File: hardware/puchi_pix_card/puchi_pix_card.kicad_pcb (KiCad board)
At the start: 4 copper layers, 54 x 54 mm, 367 parts, among them J1 USB_C_Receptacle_USB2.0_16P, J2 Conn_01x04, J3 Conn_01x10, J4 Conn_01x10, Q101 AO3401A, Q102 AO3401A, Q103 AO3401A, Q104 AO3401A, Q105 AO3401A, Q106 AO3401A, Q107 AO3401A, Q108 AO3401A, Q109 AO3401A, Q110 AO3401A, Q111 AO3401A, Q112 AO3401A, Q113 AO3401A, Q114 AO3401A, Q115 AO3401A, Q116 AO3401A, SW1 VBAT_SW, SW2 SW_Push, SW3 SW_Push, U1 TPS61023DRL, U101 MBI5153GP (R), U102 MBI5153GP (G), U103 MBI5153GP (B), U104 74HCT595, U105 74HCT595, U2 XC6206PxxxMR, U3 STM32G0B1CBTx, U4 XC6206PxxxMR, U5 USBLC6-2SC6, U6 KXTJ3-1057, U7 W25Q64JVSSIQ

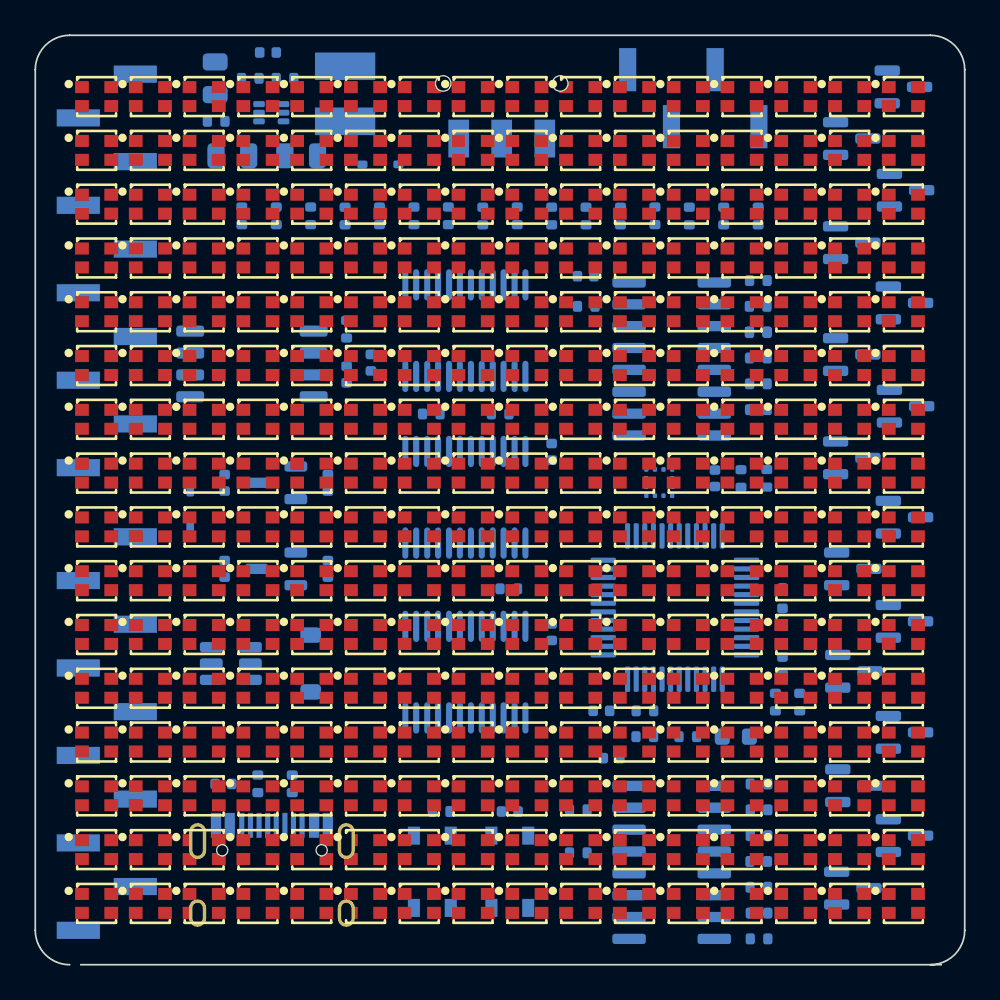
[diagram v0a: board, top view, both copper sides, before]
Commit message: Route the LED matrix lattice (F.Cu columns, In2 rows), place and route the back side, swap J1 to an SMD-shell USB-C, drop J3/J4
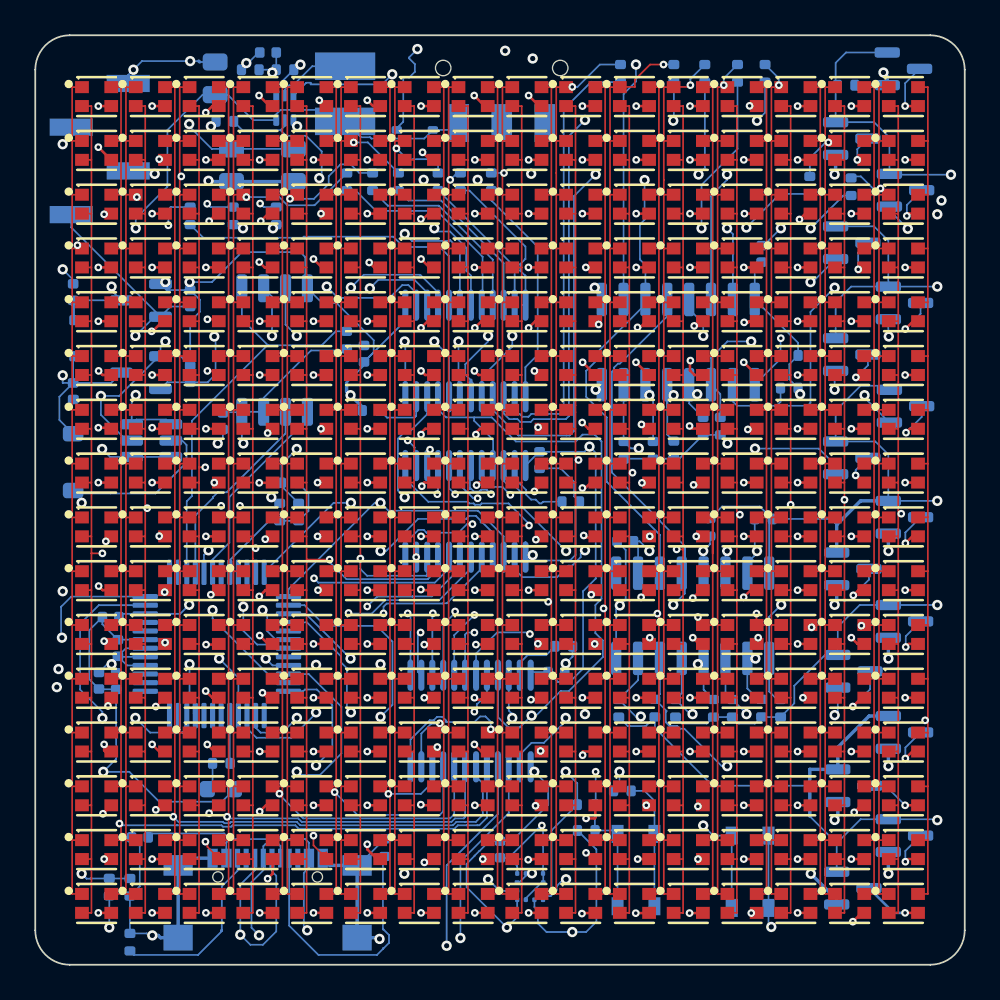
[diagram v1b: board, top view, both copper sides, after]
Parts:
- removed J3, J4: Conn_01x10, Connector_PinHeader_2.54mm:PinHeader_1x10_P2.54mm_Vertical_SMD_Pin1Left
- J1: footprint Connector_USB:USB_C_Receptacle_HRO_TYPE-C-31-M-12 -> puchi_pix_card:USB_C_Receptacle_SHOUHAN_TYPE-C-16P-QTWT
- moved R7 40.4 mm to (105.5, 149.5)
- moved R6 40.2 mm to (104.3, 149.5)
- moved C6 39.9 mm to (103.7, 137.5)
- moved C7 38.8 mm to (104.8, 135.6)
- moved C8 38.7 mm to (104.7, 137.5)
- moved J2 34.6 mm to (103.7, 106.6), turned to 0 degrees
- moved D4 30.1 mm to (110.8, 143.8)
- moved R9 27.1 mm to (110.8, 142.3), turned to 180 degrees
- moved U3 26.7 mm to (110.5, 135.4), turned to 0 degrees
- moved C12 25.8 mm to (104.4, 133.8), turned to 180 degrees
- moved C14 24.9 mm to (127.0, 147.3), turned to 90 degrees
- moved U6 24.6 mm to (128.8, 149.5)
- moved R10 24.2 mm to (114.2, 127.7), turned to -90 degrees
- moved R11 24.0 mm to (115.3, 127.7), turned to 90 degrees
- moved R14 23.0 mm to (132.0, 146.2), turned to 180 degrees
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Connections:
- U3 pad 1: /mcu/PC13 -> unconnected-(U3-PC13-Pad1)
- U3 pad 13: Net-(J3-Pin_3) -> unconnected-(U3-PA2-Pad13)
- U3 pad 14: Net-(J3-Pin_4) -> unconnected-(U3-PA3-Pad14)
- U3 pad 19: Net-(J3-Pin_6) -> unconnected-(U3-PB0-Pad19)
- U3 pad 2: /mcu/PC14 -> unconnected-(U3-PC14-Pad2)
- U3 pad 21: Net-(J3-Pin_7) -> unconnected-(U3-PB2-Pad21)
- U3 pad 22: Net-(J4-Pin_5) -> unconnected-(U3-PB10-Pad22)
- U3 pad 23: Net-(J4-Pin_6) -> unconnected-(U3-PB11-Pad23)
- U3 pad 3: /mcu/PC15 -> unconnected-(U3-PC15-Pad3)
- U3 pad 37: Net-(J3-Pin_5) -> unconnected-(U3-PA15-Pad37)
- U3 pad 42: Net-(J3-Pin_8) -> unconnected-(U3-PB3-Pad42)
- U3 pad 43: Net-(J3-Pin_9) -> unconnected-(U3-PB4-Pad43)
- U3 pad 44: Net-(J3-Pin_10) -> unconnected-(U3-PB5-Pad44)
- U3 pad 47: Net-(J4-Pin_3) -> unconnected-(U3-PB8-Pad47)
- U3 pad 48: Net-(J4-Pin_4) -> unconnected-(U3-PB9-Pad48)
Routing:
- net +5V: track 0.00 -> 416.3 mm, vias 0 -> 13
- net MBI_LE: track 0.00 -> 170.3 mm, vias 0 -> 6
- net GND: track 0.00 -> 162.2 mm, vias 0 -> 26
- net MBI_DCLK: track 0.00 -> 158.6 mm, vias 0 -> 5
- net Net-(J2-Pin_1): track 0.00 -> 102.8 mm, vias 0 -> 5
- net SR_SRCLK: track 0.00 -> 100.0 mm, vias 0 -> 4
- net /display/COL_G0: track 0.00 -> 87.1 mm, vias 0 -> 3
- net /display/COL_B15: track 0.00 -> 85.4 mm, vias 0 -> 2
- net SR_SER: track 0.00 -> 83.1 mm, vias 0 -> 2
- net /mcu/PA12: track 0.00 -> 82.5 mm, vias 0 -> 4
- net /display/COL_G15: track 0.00 -> 81.9 mm, vias 0 -> 2
- net /display/COL_G1: track 0.00 -> 81.1 mm, vias 0 -> 3
- net /display/COL_B14: track 0.00 -> 80.8 mm, vias 0 -> 2
- net /display/COL_B0: track 0.00 -> 80.8 mm, vias 0 -> 1
- net /mcu/BOOT/SWCLK: track 0.00 -> 79.5 mm, vias 0 -> 3
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- added copper zone on In1.Cu, net GND
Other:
- outline, holes or cut-outs redrawn

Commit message: Unify vias to 0.45/0.2, move decoupling caps next to their pins, tidy LED silkscreen
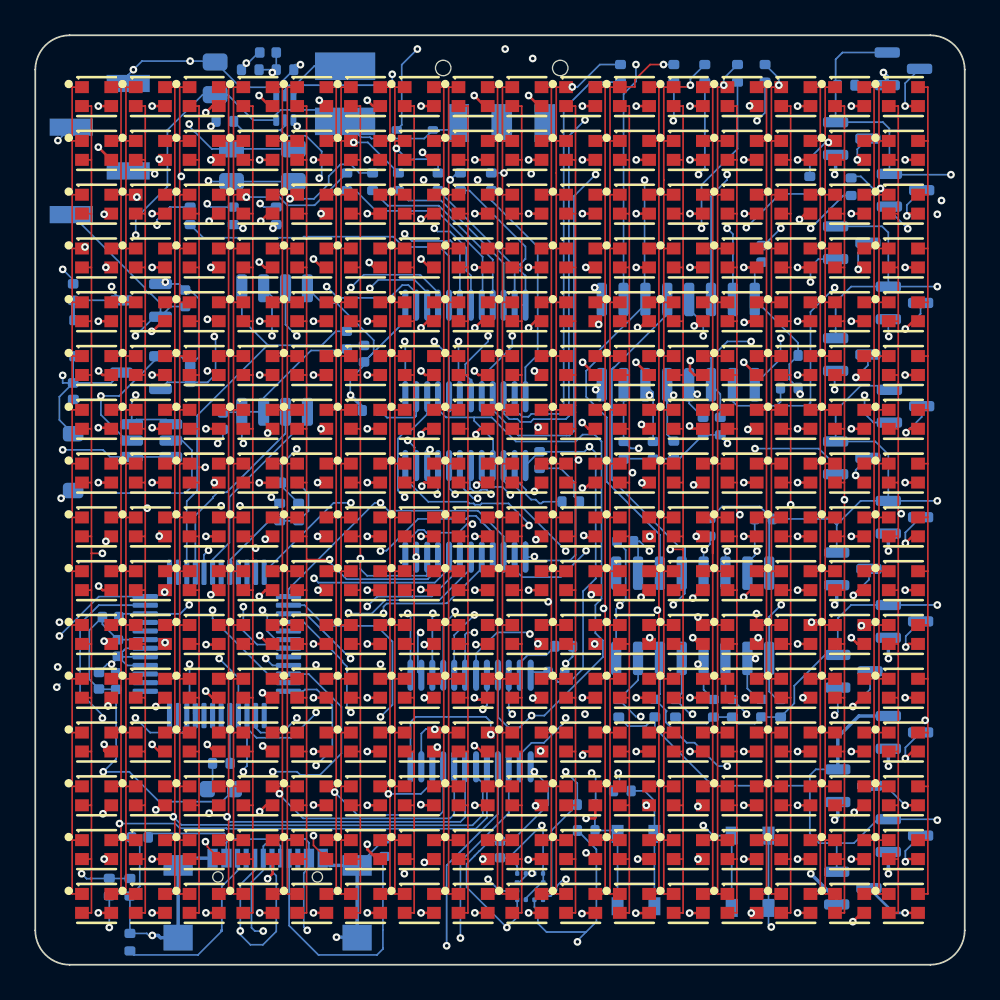
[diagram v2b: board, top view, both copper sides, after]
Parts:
- moved C5 0.30 mm to (108.7, 115.3)
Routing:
- net SR_NOE: track 62.0 -> 140.3 mm, vias 3 -> 4
- net GND: track 162.2 -> 155.1 mm, vias 26 -> 24
- net +5V: track 416.3 -> 422.0 mm
- net /mcu/PB7: track 66.0 -> 68.6 mm
- net /mcu/SWDIO: track 43.2 -> 45.6 mm
- net Net-(U101-SDO): track 26.6 -> 24.6 mm
- net Net-(J2-Pin_1): track 102.8 -> 104.6 mm
- net /mcu/PA11: track 75.2 -> 73.6 mm
- net /mcu/PA12: track 82.5 -> 84.0 mm
- net /display/COL_R2: track 62.2 -> 63.7 mm
- net SR_SER: track 83.1 -> 81.8 mm
- net /display/ROW3: track 62.9 -> 61.8 mm
- net Net-(U101-OUT11): track 34.7 -> 35.9 mm
- net +3V3P: track 79.0 -> 80.1 mm
- net /display/COL_B15: track 85.4 -> 84.3 mm
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
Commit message: Add POWER netclass (0.3mm) and set signal tracks to 0.1mm; close the boost and MCU ground loops on B.Cu
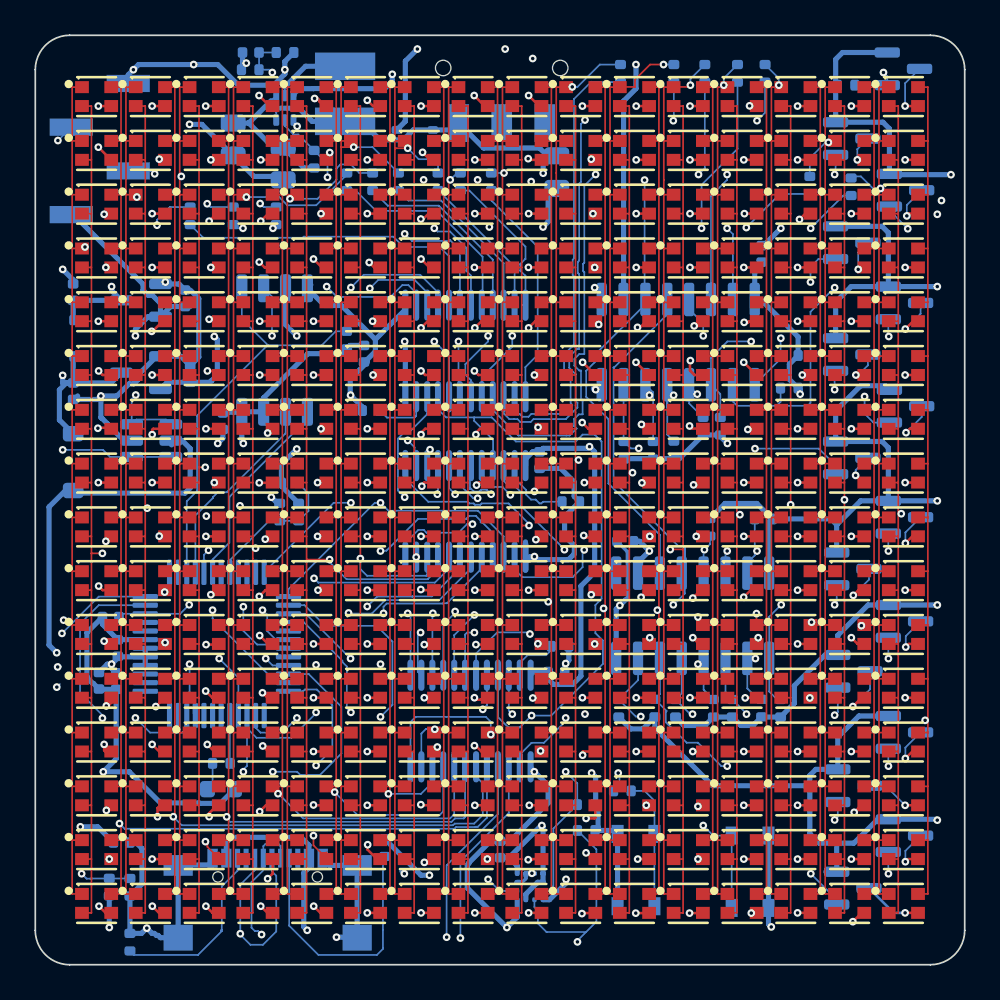
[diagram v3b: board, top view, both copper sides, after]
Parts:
- moved C1 20.6 mm to (130.3, 108.0), turned to -90 degrees
- moved R3 5.64 mm to (116.2, 107.2), turned to -90 degrees
- moved C3 1.50 mm to (111.5, 106.0), turned to 90 degrees
- moved C11 1.10 mm to (105.0, 146.9), turned to 0 degrees
- moved C16 1.00 mm to (112.5, 101.0)
- moved R2 1.00 mm to (114.5, 101.0)
- moved C2 0.61 mm to (114.4, 107.5), turned to 90 degrees
- moved R103 0.22 mm to (130.5, 135.5)
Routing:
- net Net-(D2-A): track 54.5 -> 74.0 mm, vias 2 -> 3
- net GND: track 155.1 -> 160.2 mm
- net /mcu/BOOST_EN: track 56.7 -> 52.6 mm
- net +5V: track 422.0 -> 419.4 mm
- net /display/COL_B11: track 77.3 -> 75.1 mm
- net /display/ROW13: track 62.0 -> 64.0 mm
- net /mcu/PA11: track 73.6 -> 72.1 mm
- net Net-(J2-Pin_1): track 104.6 -> 103.2 mm
- net /mcu/PA12: track 84.0 -> 82.6 mm
- net /mcu/VBUS: track 69.6 -> 68.4 mm, vias 3 -> 4
- net +3V3P: track 80.1 -> 81.1 mm
- net Net-(U101-OUT11): track 35.9 -> 36.8 mm
- net /display/ROW0: track 64.8 -> 65.7 mm
- net Net-(U1-FB): track 6.17 -> 7.07 mm
- net /display/ROW14: track 67.3 -> 66.4 mm
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
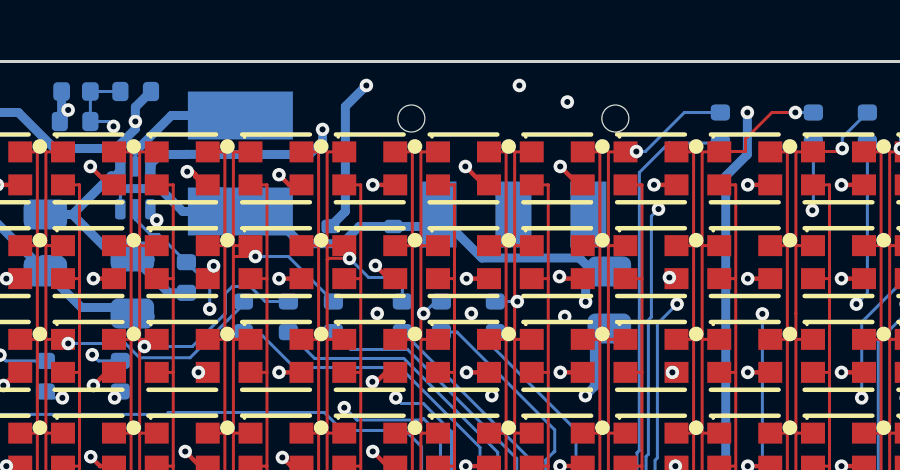
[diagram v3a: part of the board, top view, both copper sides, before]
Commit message: Bridge the +5V trunk along the top edge (0.59 -> 0.17 ohm to the first PFET)
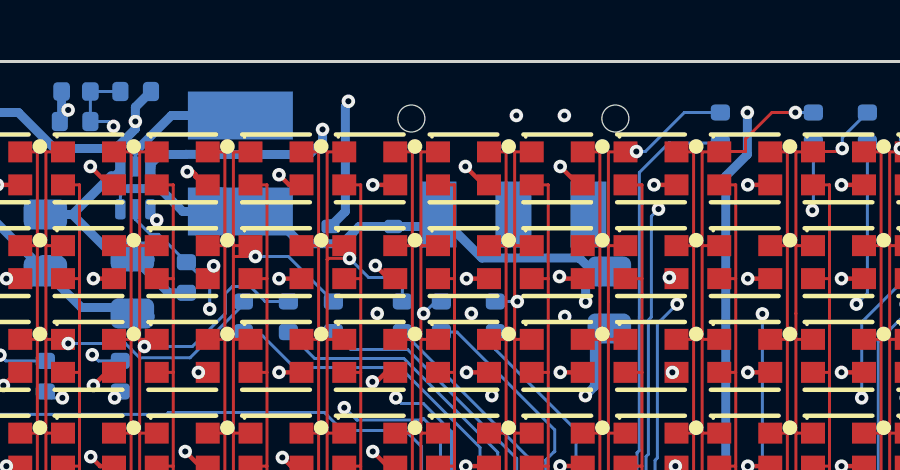
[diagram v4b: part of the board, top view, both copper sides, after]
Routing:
- net +5V: track 419.4 -> 434.1 mm
- net Net-(D2-K): track 44.6 -> 43.5 mm
- net SR_SER: track 81.5 -> 82.2 mm

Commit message: Add the Puchi-Pix logo and product name to the back silkscreen
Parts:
- added LOGO1: , brand:puchi_pix_logo, B.Cu at (137.3, 106.6)
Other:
- board text added: "Puchi-Pix"
- board text added: "V0.9"
